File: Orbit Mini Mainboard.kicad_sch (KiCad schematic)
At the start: 4 parts

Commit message: 1
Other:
- removed sheet PCIe M2
- sheet CM5 ports: added none; removed PCIE_CLK_N, PCIE_CLK_P, PCIE_PWR_EN, PCIE_RX_N, PCIE_RX_P, PCIE_TX_N, PCIE_TX_P, PCIE_nCLKREQ, PCIE_nRST, PCIE_nWAKE
- note removed: "Connectors ------ M2 MKey"

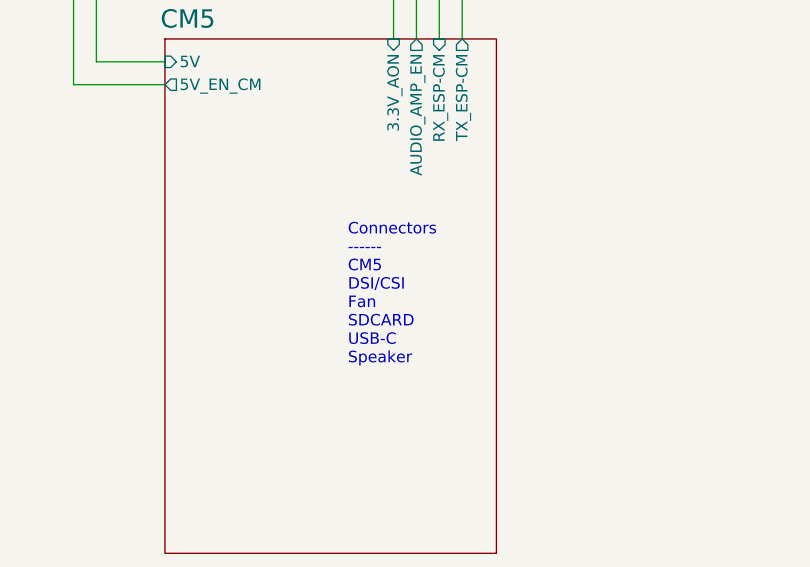
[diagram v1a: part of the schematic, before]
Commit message: micro hdmi eklendi
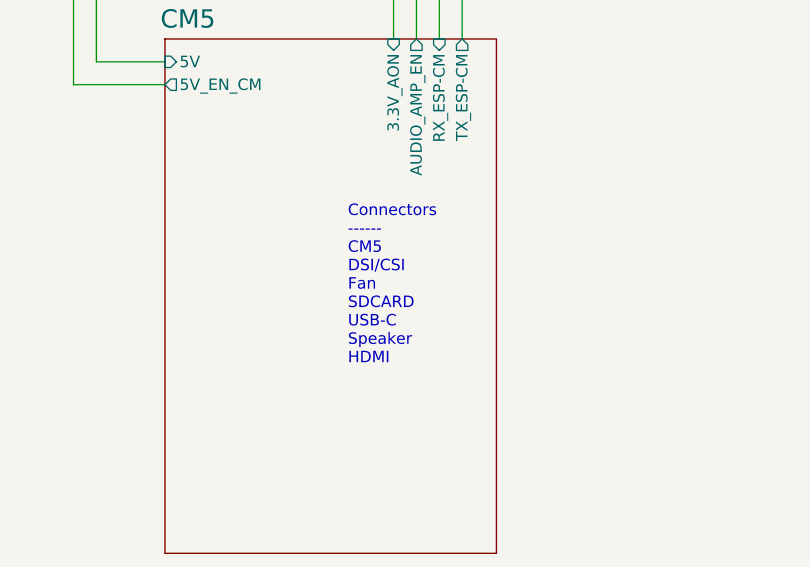
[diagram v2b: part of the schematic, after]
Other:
- note added: "Connectors ------ CM5 DSI/CSI Fan SDCARD USB-C Speaker HDMI"
- note removed: "Connectors ------ CM5 DSI/CSI Fan SDCARD USB-C Speaker"
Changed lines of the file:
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@@
 		)
 	)
-	(text "Connectors\n------\nCM5\nDSI/CSI\nFan\nSDCARD\nUSB-C\nSpeaker\n"
+	(text "Connectors\n------\nCM5\nDSI/CSI\nFan\nSDCARD\nUSB-C\nSpeaker\nHDMI"
 		(exclude_from_sim no)
 		(at 121.92 141.732 0)
